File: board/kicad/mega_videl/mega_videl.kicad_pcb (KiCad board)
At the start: 10 copper layers, 67.6 x 89 mm, 333 parts, among them J1 Conn_02x07_Odd_Even, J2 Conn_01x04, J3 FPGA JTAG, J4 Conn_01x04, J5 Conn_02x25_Odd_Even, J6 Conn_02x25_Odd_Even, U1 TPS51200DRCR, U10 5CGXFC5C6F23I7N, U11 TXV0108RGYR, U12 USB3300-EZK, U13 AP2553AW6-7, U14 PI6CG33201CZDIEX, U15 LAN9220-ABZJ, U16 PCA9546APWR, U17 HC-USB3.0-L168-WP, U18 CDCBT1001DPWR, U19 N25Q/MT25Q, U2 MT41K256M16LY, U20 TMDS1204IRNQR, U21 TPD4E02B04DQA, U22 TPD4E02B04DQA, U3 MT41K256M16LY, U4 TPS62903RPJR, U5 SN74LVC3G34DCUR, U6 TPS7A2025PDBVR, U7 TXB0104RGYR, U8 TPS62903RPJR, U9 74.25MHz, Y1 24MHz, Y2 25MHz, Y3 25MHz, Y4 ASE-50MHz

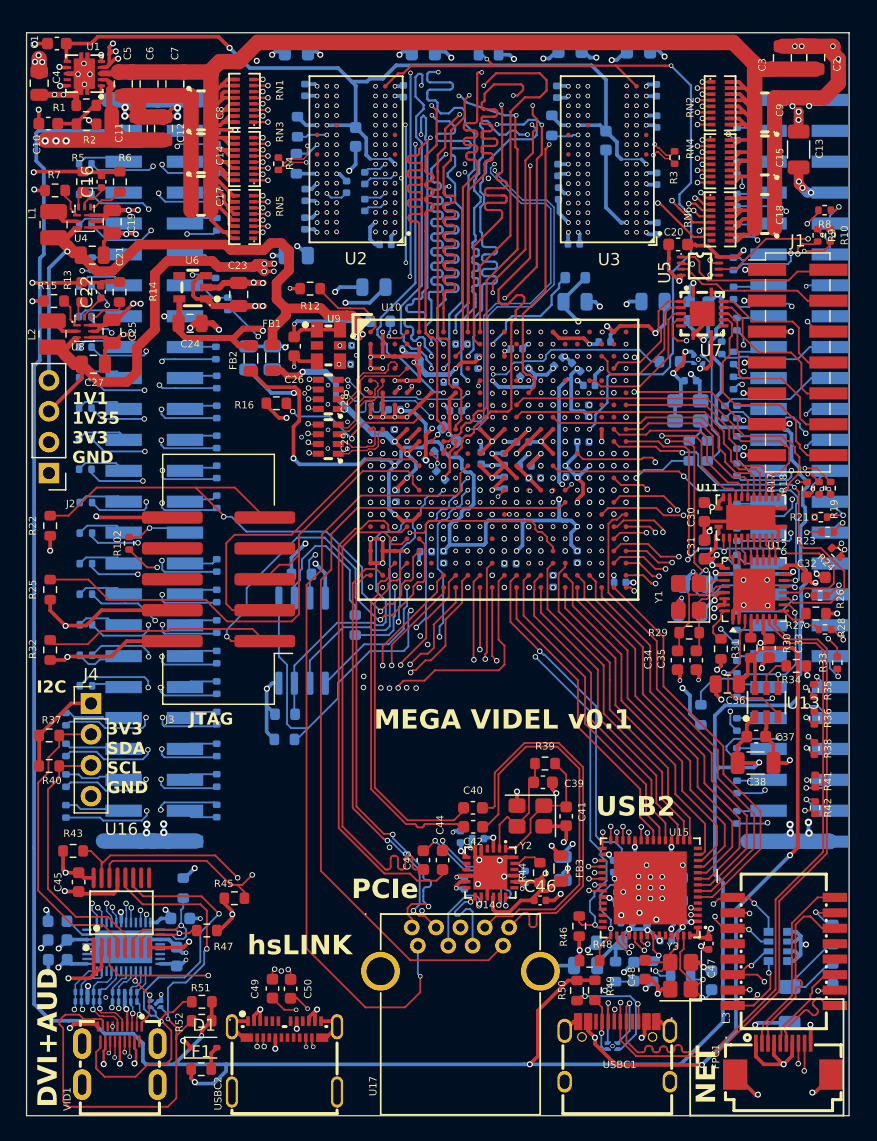
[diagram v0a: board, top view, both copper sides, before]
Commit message: Shrunk the dimensions to fit better so it does not hit Q1. Added a notch for the DIMM casing.
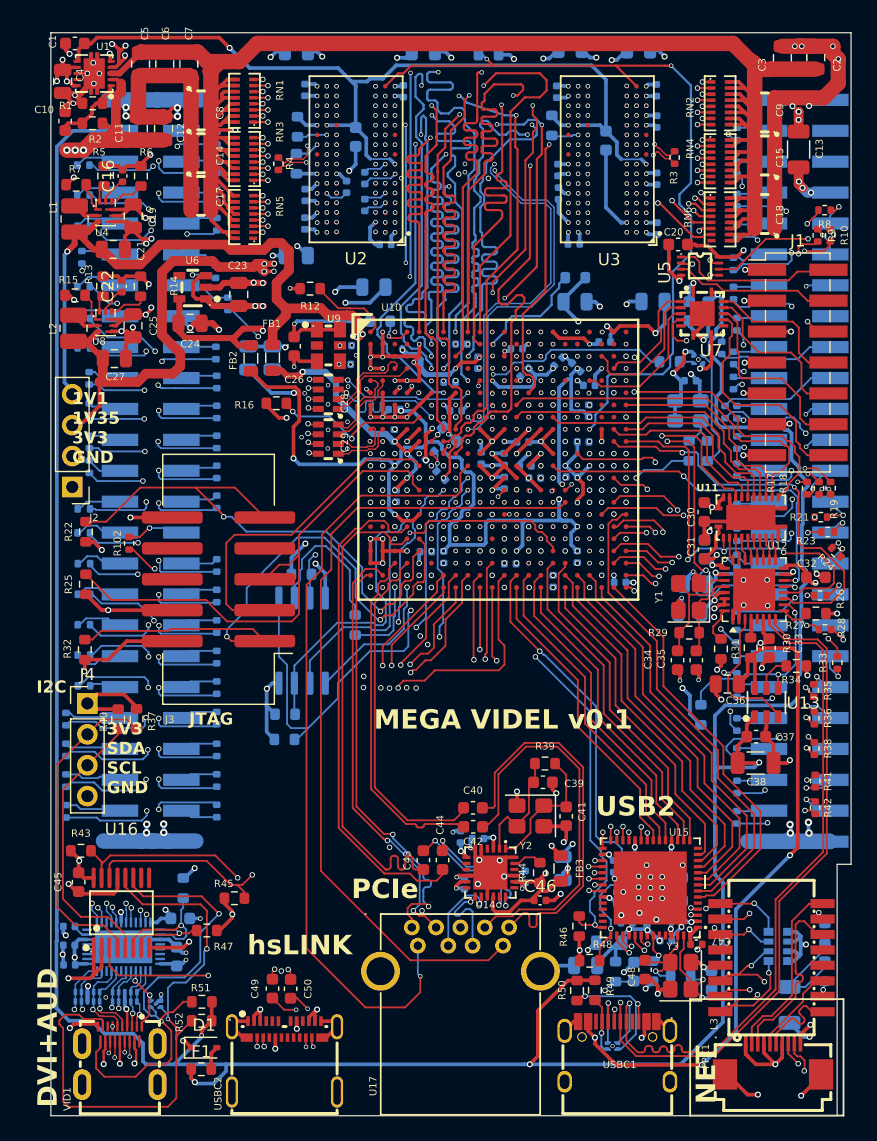
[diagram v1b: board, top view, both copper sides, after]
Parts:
- C128, C130, C133: footprint Capacitor_SMD:C_0603_1608Metric -> Capacitor_SMD:C_0402_1005Metric
- moved R37 7.31 mm to (38.5, 80.4), turned to 90 degrees
- moved R40 6.85 mm to (37.0, 80.4), turned to 90 degrees
- moved R22 2.98 mm to (34.4, 65.0)
- moved R25 2.97 mm to (34.4, 69.3)
- moved R32 2.85 mm to (34.3, 74.7)
- moved J2 2.23 mm to (33.3, 61.3)
- moved C5 2.17 mm to (38.9, 26.6)
- moved C6 2.09 mm to (40.9, 26.6)
- moved C7 2.00 mm to (42.8, 26.6)
- moved C4 1.94 mm to (32.5, 28.0)
- moved C16 1.79 mm to (37.4, 35.8)
- moved C19 1.79 mm to (38.3, 39.1)
- moved C21 1.79 mm to (36.6, 41.8)
- moved C22 1.79 mm to (37.3, 44.8)
- moved L1 1.79 mm to (33.5, 39.3)
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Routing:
- net +1V35: track 188.9 -> 168.3 mm, vias 69 -> 67
- net GND: track 488.1 -> 476.6 mm, vias 300 -> 297
- net +5V: track 246.7 -> 241.9 mm
- net +3V3: track 167.9 -> 163.9 mm, vias 82 -> 79
- net /fpga/TCK: track 52.5 -> 49.3 mm
- net /fpga/TMS: track 47.3 -> 44.5 mm
- net /fpga/TDI: track 49.1 -> 46.4 mm
- net /Ethernet/TPO_N: track 23.0 -> 25.4 mm
- net Net-(L3-RCT): track 27.4 -> 29.7 mm
- net +1V1: track 108.2 -> 106.4 mm
- net /video/EXT.SDA: track 25.0 -> 26.8 mm
- net Net-(L3-TXCT): track 3.43 -> 1.82 mm
- net /Ethernet/TPO_P: track 20.9 -> 22.5 mm
- net /fpga/CT.RST_N: track 67.9 -> 69.4 mm
- net /fpga/CT.D15: track 27.0 -> 25.6 mm
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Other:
- board size 67.6 x 89 mm -> 65.8 x 89 mm
